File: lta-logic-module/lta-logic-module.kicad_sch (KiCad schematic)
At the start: 15 parts

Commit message: More unfucking.
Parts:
- removed J2: (no value), symbol Connector:Conn_01x01_Female
- J1: symbol Connector:Conn_01x01_Female -> Aaron-Connectors:Molex-MicroFit_43650-0218; MANUFACTURER (none) -> Molex; MPN XXX TODO FIND -> 436500218
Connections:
- net GND: now also J1.2
- no-connect marks 19 -> 21
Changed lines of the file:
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@@
   (no_connect (at 64.135 66.675))
   (no_connect (at 64.135 61.595))
+  (no_connect (at 27.94 27.94))
+  (no_connect (at 27.94 30.48))
   (no_connect (at 93.345 86.995))
   (wire (pts (xy 125.095 76.2) (xy 125.095 75.565))
@@
     (stroke (width 0) (type default) (color 0 0 0 0))
   )
-  (wire (pts (xy 27.94 29.845) (xy 39.37 29.845))
-    (stroke (width 0) (type default) (color 0 0 0 0))
-  )
   (wire (pts (xy 143.51 186.69) (xy 139.7 186.69))
     (stroke (width 0) (type default) (color 0 0 0 0))
@@
     (stroke (width 0) (type default) (color 0 0 0 0))
   )
+  (wire (pts (xy 27.94 25.4) (xy 39.37 25.4))
+    (stroke (width 0) (type default) (color 0 0 0 0))
+  )
   (wire (pts (xy 116.84 70.485) (xy 125.095 70.485))
     (stroke (width 0) (type default) (color 0 0 0 0))
@@
     (stroke (width 0) (type default) (color 0 0 0 0))
   )
-  (wire (pts (xy 39.37 29.845) (xy 39.37 32.385))
+  (wire (pts (xy 39.37 25.4) (xy 39.37 32.385))
     (stroke (width 0) (type default) (color 0 0 0 0))
   )
@@
     )
     (property "Datasheet" "" (id 3) (at 100.33 113.665 0)
-      (effects (font (size 1.27 1.27)) hide)
-    )
-    (pin "1")
-  )
-  (symbol (lib_id "Connector:Conn_01x01_Female") (at 22.86 29.845 180) (unit 1)
-    (in_bom yes) (on_board yes) (fields_autoplaced)
-    (property "Reference" "J2" (id 0) (at 23.495 25.688 0))
-    (property "Value" "" (id 1) (at 23.495 28.2249 0))
-    (property "Footprint" "" (id 2) (at 22.86 29.845 0)
-      (effects (font (size 1.27 1.27)) hide)
-    )
-    (property "Datasheet" "~" (id 3) (at 22.86 29.845 0)
-      (effects (font (size 1.27 1.27)) hide)
-    )
-    (property "Comment" "TODO REPLACE FOOTPRINT" (id 4) (at 22.86 29.845 0)
-      (effects (font (size 1.27 1.27)) hide)
-    )
-    (property "MPN" "XXX TODO FIND" (id 5) (at 22.86 29.845 0)
       (effects (font (size 1.27 1.27)) hide)
     )
@@
     (pin "1")
   )
-  (symbol (lib_id "Connector:Conn_01x01_Female") (at 22.86 22.86 180) (unit 1)
-    (in_bom yes) (on_board yes) (fields_autoplaced)
-    (property "Reference" "J1" (id 0) (at 23.495 18.703 0))
-    (property "Value" "" (id 1) (at 23.495 21.2399 0))
-    (property "Footprint" "" (id 2) (at 22.86 22.86 0)
-      (effects (font (size 1.27 1.27)) hide)
-    )
-    (property "Datasheet" "~" (id 3) (at 22.86 22.86 0)
-      (effects (font (size 1.27 1.27)) hide)
-    )
-    (property "Comment" "TODO REPLACE FOOTPRINT" (id 4) (at 22.86 22.86 0)
-      (effects (font (size 1.27 1.27)) hide)
-    )
-    (property "MPN" "XXX TODO FIND" (id 5) (at 22.86 22.86 0)
-      (effects (font (size 1.27 1.27)) hide)
-    )
-    (pin "1")
+  (symbol (lib_id "Aaron-Connectors:Molex-MicroFit_43650-0218") (at 27.94 22.86 0) (mirror y) (unit 1)
+    (in_bom yes) (on_board yes)
+    (property "Reference" "J1" (id 0) (at 18.415 19.05 0))
+    (property "Value" "" (id 1) (at 13.335 28.575 90))
+    (property "Footprint" "" (id 2) (at 17.78 36.83 0)
+      (effects (font (size 1.524 1.524)) hide)
+    )
+    (property "Datasheet" "https://www.molex.com/pdm_docs/ps/PS-43650.pdf" (id 3) (at 19.05 19.05 0)
+      (effects (font (size 1.524 1.524)) hide)
+    )
+    (property "Comment" "TODO REPLACE FOOTPRINT" (id 4) (at 27.94 22.86 0)
+      (effects (font (size 1.27 1.27)) hide)
+    )
+    (property "MPN" "436500218" (id 5) (at 8.89 27.94 0)
+      (effects (font (size 1.27 1.27)) hide)
+    )
+    (property "MANUFACTURER" "Molex" (id 6) (at 11.43 25.4 0)
+      (effects (font (size 1.27 1.27)) hide)
+    )
+    (pin "1")
+    (pin "2")
+    (pin "P1")
+    (pin "P2")
   )
   (symbol (lib_id "power:GND") (at 39.37 32.385 0) (unit 1)
@@
       (reference "C4") (unit 1) (value "4u7") (footprint "Capacitor_SMD:C_0805_2012Metric")
     )
-    (path "/e5533935-513b-40ea-969d-0b26d3cce6c4/1ff7436d-9ad6-4fc1-a499-76d3565a3e56"
+    (path "/e5533935-513b-40ea-969d-0b26d3cce6c4/48db8a47-7935-4b28-804d-5463b23d6e3a"
       (reference "C5") (unit 1) (value "220u") (footprint "Capacitor_THT:CP_Radial_D8.0mm_P3.50mm")
     )
@@
     )
     (path "/b22c9ebe-66d4-4188-b4db-cbd1721541a8"
-      (reference "J1") (unit 1) (value "Conn_01x01_Female") (footprint "Connector_PinHeader_2.54mm:PinHeader_1x01_P2.54mm_Vertical")
-    )
-    (path "/4fc78570-8db8-4eb9-adcc-368a5720826a"
-      (reference "J2") (unit 1) (value "Conn_01x01_Female") (footprint "Connector_PinHeader_2.54mm:PinHeader_1x01_P2.54mm_Vertical")
+      (reference "J1") (unit 1) (value "Molex-MicroFit_43650-0218") (footprint "Aaron_THT:Molex-Microfit-43650-0218")
     )
     (path "/5aae325f-8866-4428-9c3a-cbc77f646a49/4799fb37-e41f-4613-89ed-b23d12b6c343"

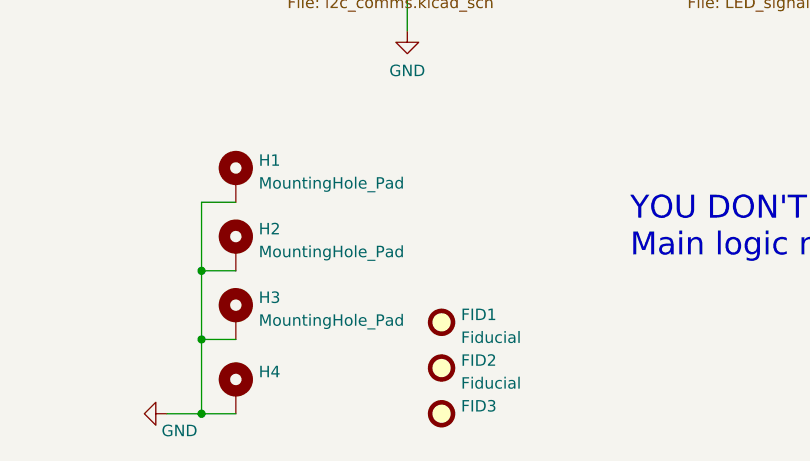
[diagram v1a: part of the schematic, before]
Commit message: Switch 12-pin headers to Molex Micro-Latch c'tors.
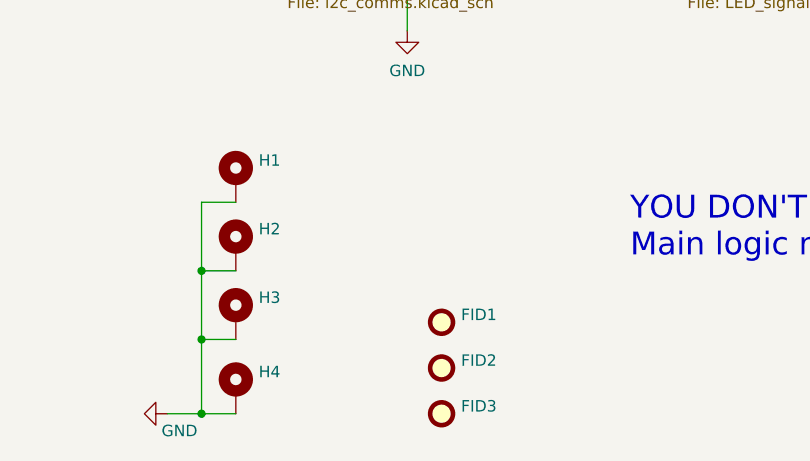
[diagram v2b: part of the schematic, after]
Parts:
- FID1, FID2: value Fiducial -> (none); footprint Fiducial:Fiducial_1mm_Mask2mm -> (none)
- H1, H2, H3: value MountingHole_Pad -> (none); footprint MountingHole:MountingHole_2.2mm_M2_ISO7380_Pad -> (none)
- J1: Comment TODO REPLACE FOOTPRINT -> (none)
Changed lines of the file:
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@@
       (effects (font (size 1.27 1.27)) (justify left))
     )
-    (property "Value" "Fiducial" (id 1) (at 168.529 191.5672 0)
-      (effects (font (size 1.27 1.27)) (justify left))
-    )
-    (property "Footprint" "Fiducial:Fiducial_1mm_Mask2mm" (id 2) (at 166.37 189.865 0)
+    (property "Value" "" (id 1) (at 168.529 191.5672 0)
+      (effects (font (size 1.27 1.27)) (justify left))
+    )
+    (property "Footprint" "" (id 2) (at 166.37 189.865 0)
       (effects (font (size 1.27 1.27)) hide)
     )
@@
       (effects (font (size 1.27 1.27)) (justify left))
     )
-    (property "Value" "Fiducial" (id 1) (at 168.529 186.4872 0)
-      (effects (font (size 1.27 1.27)) (justify left))
-    )
-    (property "Footprint" "Fiducial:Fiducial_1mm_Mask2mm" (id 2) (at 166.37 184.785 0)
+    (property "Value" "" (id 1) (at 168.529 186.4872 0)
+      (effects (font (size 1.27 1.27)) (justify left))
+    )
+    (property "Footprint" "" (id 2) (at 166.37 184.785 0)
       (effects (font (size 1.27 1.27)) hide)
     )
@@
       (effects (font (size 1.27 1.27)) (justify left))
     )
-    (property "Value" "MountingHole_Pad" (id 1) (at 146.05 169.3422 0)
-      (effects (font (size 1.27 1.27)) (justify left))
-    )
-    (property "Footprint" "MountingHole:MountingHole_2.2mm_M2_ISO7380_Pad" (id 2) (at 143.51 168.91 0)
+    (property "Value" "" (id 1) (at 146.05 169.3422 0)
+      (effects (font (size 1.27 1.27)) (justify left))
+    )
+    (property "Footprint" "" (id 2) (at 143.51 168.91 0)
       (effects (font (size 1.27 1.27)) hide)
     )
@@
       (effects (font (size 1.27 1.27)) (justify left))
     )
-    (property "Value" "MountingHole_Pad" (id 1) (at 146.05 176.9622 0)
-      (effects (font (size 1.27 1.27)) (justify left))
-    )
-    (property "Footprint" "MountingHole:MountingHole_2.2mm_M2_ISO7380_Pad" (id 2) (at 143.51 176.53 0)
+    (property "Value" "" (id 1) (at 146.05 176.9622 0)
+      (effects (font (size 1.27 1.27)) (justify left))
+    )
+    (property "Footprint" "" (id 2) (at 143.51 176.53 0)
       (effects (font (size 1.27 1.27)) hide)
     )
@@
       (effects (font (size 1.27 1.27)) (justify left))
     )
-    (property "Value" "MountingHole_Pad" (id 1) (at 146.05 184.5822 0)
-      (effects (font (size 1.27 1.27)) (justify left))
-    )
-    (property "Footprint" "MountingHole:MountingHole_2.2mm_M2_ISO7380_Pad" (id 2) (at 143.51 184.15 0)
+    (property "Value" "" (id 1) (at 146.05 184.5822 0)
+      (effects (font (size 1.27 1.27)) (justify left))
+    )
+    (property "Footprint" "" (id 2) (at 143.51 184.15 0)
       (effects (font (size 1.27 1.27)) hide)
     )
@@
       (effects (font (size 1.524 1.524)) hide)
     )
-    (property "Comment" "TODO REPLACE FOOTPRINT" (id 4) (at 27.94 22.86 0)
+    (property "Comment" "" (id 4) (at 27.94 22.86 0)
       (effects (font (size 1.27 1.27)) hide)
     )
@@
     )
     (path "/5aae325f-8866-4428-9c3a-cbc77f646a49/4799fb37-e41f-4613-89ed-b23d12b6c343"
-      (reference "J3") (unit 1) (value "Conn_01x12") (footprint "Connector_PinHeader_2.54mm:PinHeader_1x12_P2.54mm_Vertical")
+      (reference "J3") (unit 1) (value "Molex-MicroLatch-53253-1270") (footprint "Aaron_THT:Molex-MicroLatch-53253-1270")
     )
     (path "/5aae325f-8866-4428-9c3a-cbc77f646a49/f176bd72-6f10-4297-97cf-05a5643d210f"
-      (reference "J4") (unit 1) (value "Conn_01x12") (footprint "Connector_PinHeader_2.54mm:PinHeader_1x12_P2.54mm_Vertical")
+      (reference "J4") (unit 1) (value "Molex-MicroLatch-53253-1270") (footprint "Aaron_THT:Molex-MicroLatch-53253-1270")
     )
     (path "/6c463b66-7d6a-4cf9-b3f0-191f3a7738ed/73eb0bc7-e366-4abc-ad37-2f48672e6367"
-      (reference "J5") (unit 1) (value "Conn_01x12") (footprint "Connector_PinHeader_2.54mm:PinHeader_1x12_P2.54mm_Vertical")
+      (reference "J5") (unit 1) (value "Molex-MicroLatch-53253-1270") (footprint "Aaron_THT:Molex-MicroLatch-53253-1270")
     )
     (path "/b07b5a53-95e4-46c7-beb1-5ef197e6319a/cbd8b785-0c8e-4509-ba77-b2205bc85c2c"

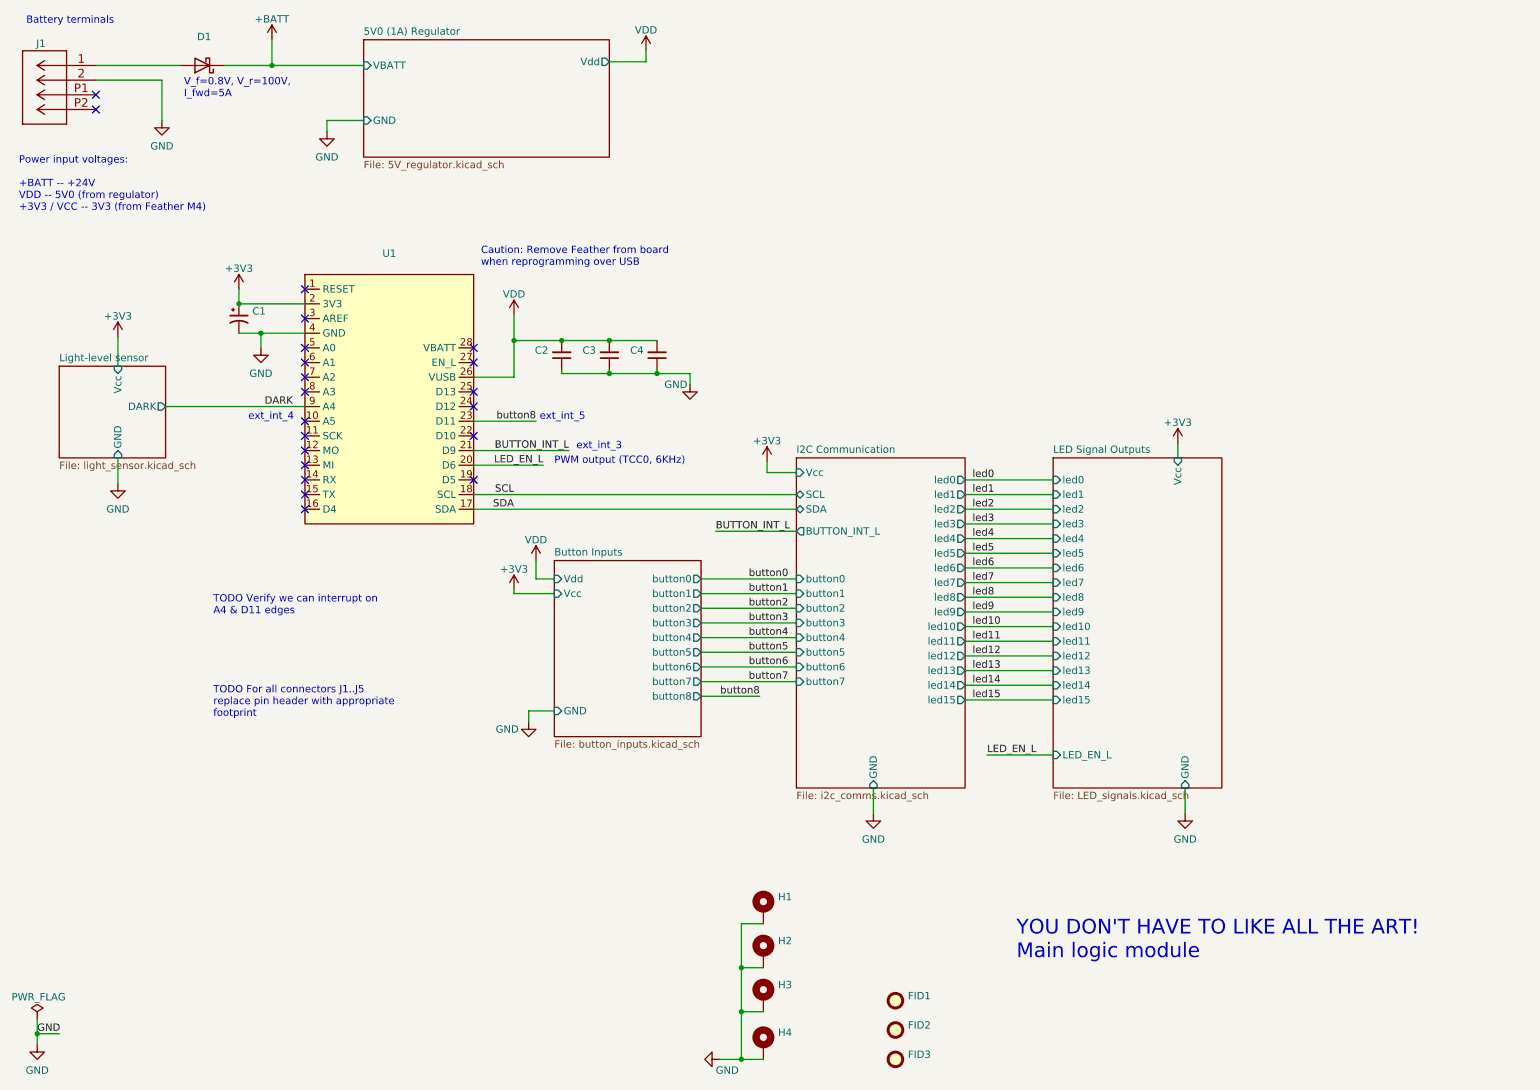
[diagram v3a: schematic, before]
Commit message: Update some footprints to be more accurate.
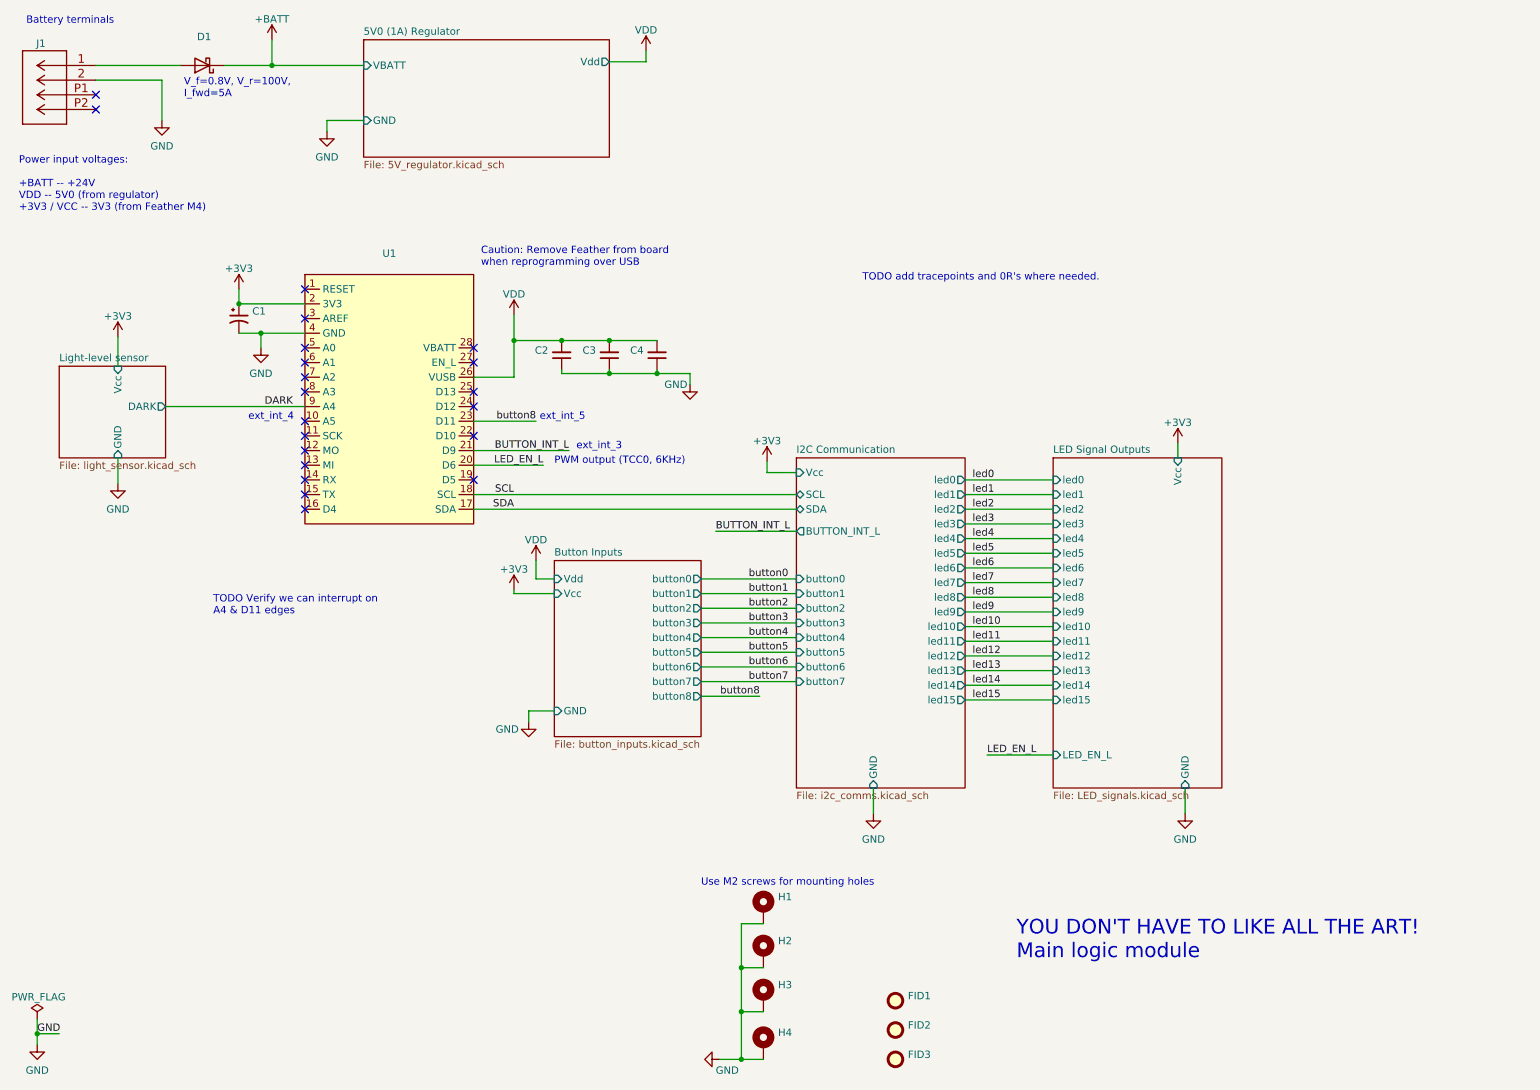
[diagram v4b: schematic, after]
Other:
- note added: "TODO add tracepoints and 0R's where needed."
- note added: "Use M2 screws for mounting holes"
- note removed: "TODO For all connectors J1..J5 replace pin header with appropriate footprint"
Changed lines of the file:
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@@
     (stroke (width 0) (type default) (color 0 0 0 0))
+  )
+  (text "TODO add tracepoints and 0R's where needed." (at 160.655 60.325 0)
+    (effects (font (size 1.27 1.27)) (justify left bottom))
   )
   (text "ext_int_5\n" (at 104.775 84.455 0)
@@
     (effects (font (size 1.27 1.27)) (justify left bottom))
   )
+  (text "Use M2 screws for mounting holes " (at 132.715 165.1 0)
+    (effects (font (size 1.27 1.27)) (justify left bottom))
+  )
   (text "TODO Verify we can interrupt on\nA4 & D11 edges" (at 48.26 118.11 0)
     (effects (font (size 1.27 1.27)) (justify left bottom))
@@
   )
   (text "PWM output (TCC0, 6KHz)" (at 107.315 92.075 0)
-    (effects (font (size 1.27 1.27)) (justify left bottom))
-  )
-  (text "TODO For all connectors J1..J5\nreplace pin header with appropriate\nfootprint"
-    (at 48.26 135.89 0)
     (effects (font (size 1.27 1.27)) (justify left bottom))
   )
@@
       (reference "J1") (unit 1) (value "Molex-MicroFit_43650-0218") (footprint "Aaron_THT:Molex-Microfit-43650-0218")
     )
+    (path "/6c463b66-7d6a-4cf9-b3f0-191f3a7738ed/73eb0bc7-e366-4abc-ad37-2f48672e6367"
+      (reference "J2") (unit 1) (value "Molex-MicroLatch-53253-1270") (footprint "Aaron_THT:Molex-MicroLatch-53253-1270")
+    )
     (path "/5aae325f-8866-4428-9c3a-cbc77f646a49/4799fb37-e41f-4613-89ed-b23d12b6c343"
       (reference "J3") (unit 1) (value "Molex-MicroLatch-53253-1270") (footprint "Aaron_THT:Molex-MicroLatch-53253-1270")
@@
       (reference "J4") (unit 1) (value "Molex-MicroLatch-53253-1270") (footprint "Aaron_THT:Molex-MicroLatch-53253-1270")
     )
-    (path "/6c463b66-7d6a-4cf9-b3f0-191f3a7738ed/73eb0bc7-e366-4abc-ad37-2f48672e6367"
-      (reference "J5") (unit 1) (value "Molex-MicroLatch-53253-1270") (footprint "Aaron_THT:Molex-MicroLatch-53253-1270")
-    )
     (path "/b07b5a53-95e4-46c7-beb1-5ef197e6319a/cbd8b785-0c8e-4509-ba77-b2205bc85c2c"
